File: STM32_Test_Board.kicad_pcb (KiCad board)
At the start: 2 copper layers, 51 x 57.5 mm, 7 parts, among them J1 Conn_01x16_Male, J2 Conn_01x16_Male, J3 Conn_01x16_Male, J4 Conn_01x16_Male, U1 STM32G484RET6

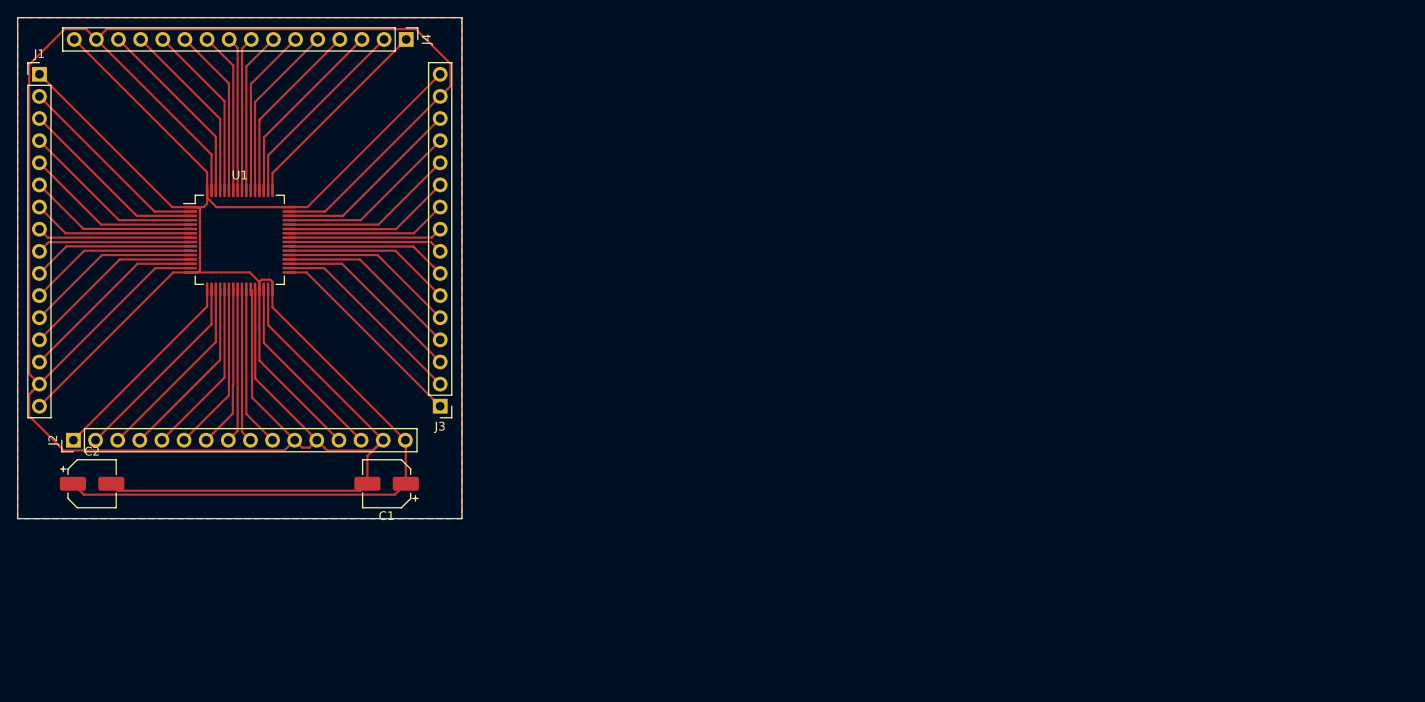
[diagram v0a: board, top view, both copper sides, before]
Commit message: Adding decoupling capacitor
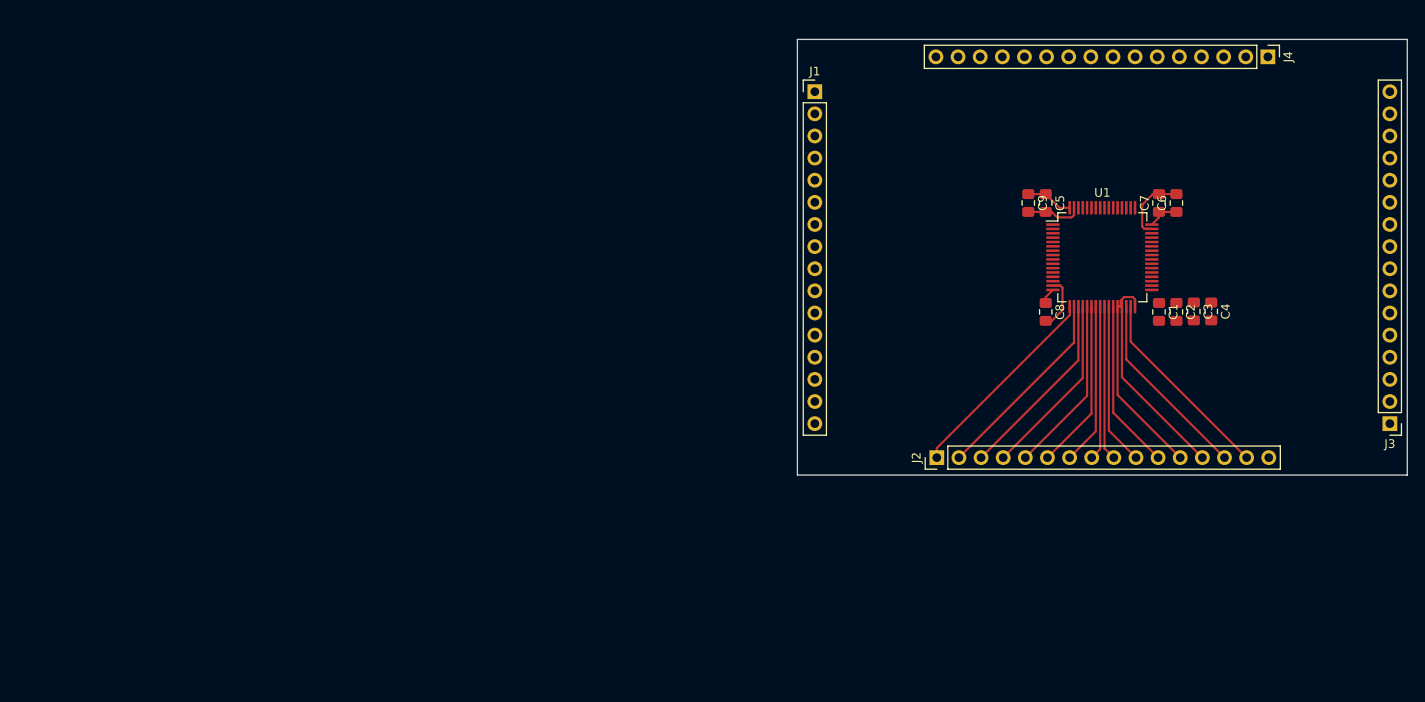
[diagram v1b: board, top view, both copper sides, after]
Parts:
- added C3: 100nF/50VDC, Capacitor_SMD:C_0805_2012Metric_Pad1.15x1.40mm_HandSolder, F.Cu at (240.5, 79.2)
- added C4: 1uF/50VDC, Capacitor_SMD:C_0805_2012Metric_Pad1.15x1.40mm_HandSolder, F.Cu at (242.5, 79.2)
- added C5: 100nF/50VDC, Capacitor_SMD:C_0805_2012Metric_Pad1.15x1.40mm_HandSolder, F.Cu at (223.5, 66.8)
- added C6: 100nF/50VDC, Capacitor_SMD:C_0805_2012Metric_Pad1.15x1.40mm_HandSolder, F.Cu at (238.5, 66.8)
- added C7: 100nF/50VDC, Capacitor_SMD:C_0805_2012Metric_Pad1.15x1.40mm_HandSolder, F.Cu at (236.5, 66.8)
- added C8: 100nF/50VDC, Capacitor_SMD:C_0805_2012Metric_Pad1.15x1.40mm_HandSolder, F.Cu at (223.5, 79.3)
- added C9: 4.7uF/50VDC, Capacitor_SMD:C_0805_2012Metric_Pad1.15x1.40mm_HandSolder, F.Cu at (221.5, 66.8)
- C1: value 100uF/50VDC -> 10nF/50VDC; footprint Capacitor_SMD:CP_Elec_5x5.4 -> Capacitor_SMD:C_0805_2012Metric_Pad1.15x1.40mm_HandSolder
- C2: footprint Capacitor_SMD:CP_Elec_5x5.4 -> Capacitor_SMD:C_0805_2012Metric_Pad1.15x1.40mm_HandSolder
- moved C2 126.0 mm to (238.5, 79.3), turned to 270 degrees
- moved J3 109.0 mm to (263.0, 92.1)
- moved J2 99.1 mm to (211.0, 96.0)
- moved U1 99.0 mm to (230.0, 73.0)
- moved J4 98.9 mm to (249.0, 50.0)
- moved C1 90.8 mm to (236.5, 79.3), turned to 270 degrees
- moved J1 89.0 mm to (197.0, 54.0)
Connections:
- J1 pad 1: 3.3V -> /1
- J2 pad 12: GND -> 3.3V
- U1 pad 1: 3.3V -> /1
- U1 pad 28: GND -> 3.3V
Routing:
- net GND: track 309.3 -> 63.1 mm
- net 3.3V: track 219.1 -> 56.5 mm
- net /49: track 23.7 -> 0.00 mm
- net /33: track 23.7 -> 0.00 mm
- net /50: track 22.8 -> 0.00 mm
- net /34: track 22.8 -> 0.00 mm
- net /2: track 22.8 -> 0.00 mm
- net /51: track 22.0 -> 0.00 mm
- net /14: track 22.0 -> 0.00 mm
- net /35: track 22.0 -> 0.00 mm
- net /62: track 22.0 -> 0.00 mm
- net /3: track 22.0 -> 0.00 mm
- net /46: track 22.0 -> 0.00 mm
- net /13: track 21.1 -> 0.00 mm
- net /52: track 21.1 -> 0.00 mm
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- removed copper zone on F.Cu, net (none)
- removed copper zone on F.Cu, net GND
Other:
- board size 51 x 57.5 mm -> 70 x 50 mm

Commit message: Exporting fabrication files
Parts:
- added REF**: MountingHole_2.2mm_M2_Pad, MountingHole:MountingHole_2.2mm_M2_Pad, F.Cu at (121.0, 117.0)
- added REF**: MountingHole_2.2mm_M2_Pad, MountingHole:MountingHole_2.2mm_M2_Pad, F.Cu at (171.0, 117.0)
- added REF**: MountingHole_2.2mm_M2_Pad, MountingHole:MountingHole_2.2mm_M2_Pad, F.Cu at (121.0, 77.0)
- added REF**: MountingHole_2.2mm_M2_Pad, MountingHole:MountingHole_2.2mm_M2_Pad, F.Cu at (171.0, 77.0)
- moved C1 87.4 mm to (152.5, 103.3)
- moved C2 87.4 mm to (154.5, 103.3)
- moved C3 87.4 mm to (156.5, 103.2)
- moved C4 87.4 mm to (158.5, 103.2)
- moved C5 87.4 mm to (139.5, 90.8)
- moved C6 87.4 mm to (154.5, 90.8)
- moved C7 87.4 mm to (152.5, 90.8)
- moved C8 87.4 mm to (139.5, 103.3)
- moved C9 87.4 mm to (137.5, 90.8)
- moved J1 87.4 mm to (113.0, 78.0)
- moved J2 87.4 mm to (127.0, 120.0)
- moved J3 87.4 mm to (179.0, 116.1)
- moved J4 87.4 mm to (165.0, 74.0)
- moved U1 87.4 mm to (146.0, 97.0)
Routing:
- net 3.3V: track 56.5 -> 403.8 mm
- net GND: track 63.1 -> 204.3 mm
- net /33: track 0.00 -> 33.7 mm
- net /1: track 0.00 -> 33.6 mm
- net /34: track 0.00 -> 32.8 mm
- net /2: track 0.00 -> 32.8 mm
- net /14: track 0.00 -> 32.0 mm
- net /35: track 0.00 -> 32.0 mm
- net /46: track 0.00 -> 32.0 mm
- net /3: track 0.00 -> 32.0 mm
- net /36: track 0.00 -> 31.1 mm
- net /13: track 0.00 -> 31.1 mm
- net /45: track 0.00 -> 31.1 mm
- net /4: track 0.00 -> 31.1 mm
- net /37: track 0.00 -> 30.3 mm
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- added copper zone on F.Cu, net (none)
- added copper zone on F.Cu, net GND
